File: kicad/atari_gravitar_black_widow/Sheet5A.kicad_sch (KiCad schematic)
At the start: 121 parts, among them Q2 2N6044, Q3 2N6044, Q4 2N6044

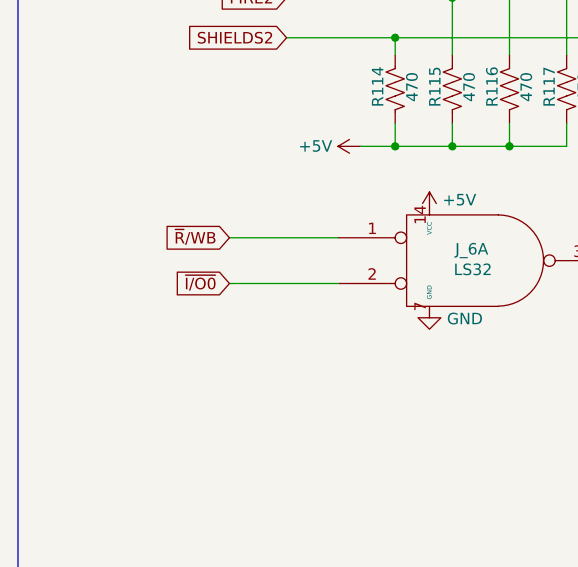
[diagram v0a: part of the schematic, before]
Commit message: Row 3 - 3.5 tracess
Also fixed some schematic errors (IO at J6, power at R4, Z out TP)
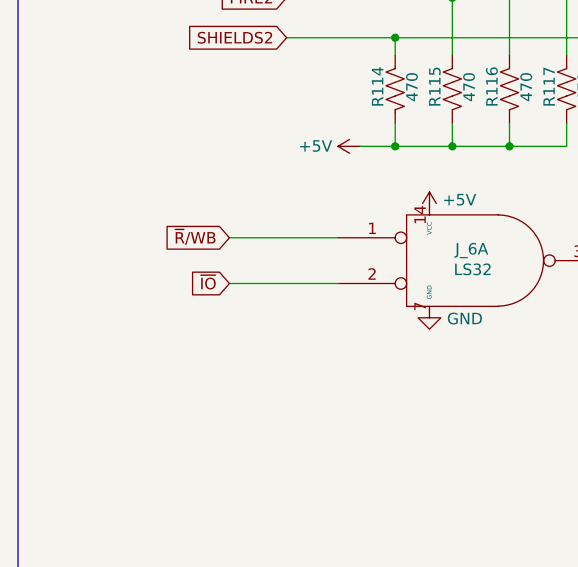
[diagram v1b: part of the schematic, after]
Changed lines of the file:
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@@
     )
   )
-  (global_label "~{I{slash}O0}" (shape input) (at 61.595 146.05 180) (fields_autoplaced)
+  (global_label "~{IO}" (shape input) (at 61.595 146.05 180) (fields_autoplaced)
     (effects (font (size 1.27 1.27)) (justify right))
-    (property "Intersheet References" "${INTERSHEET_REFS}" (id 0) (at 54.7956 145.9706 0)
+    (property "Intersheet References" "${INTERSHEET_REFS}" (id 0) (at 57.3356 145.9706 0)
       (effects (font (size 1.27 1.27)) (justify right) hide)
     )

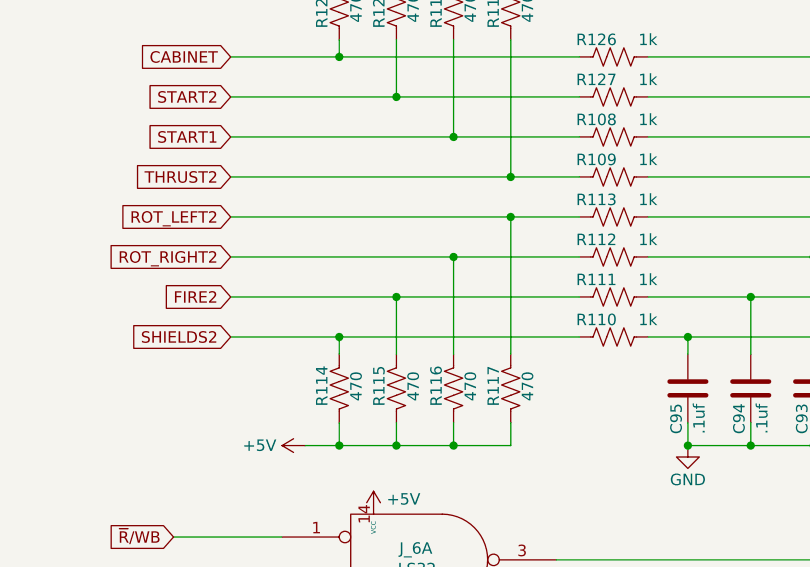
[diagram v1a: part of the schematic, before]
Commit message: fixed coin door schematic issues
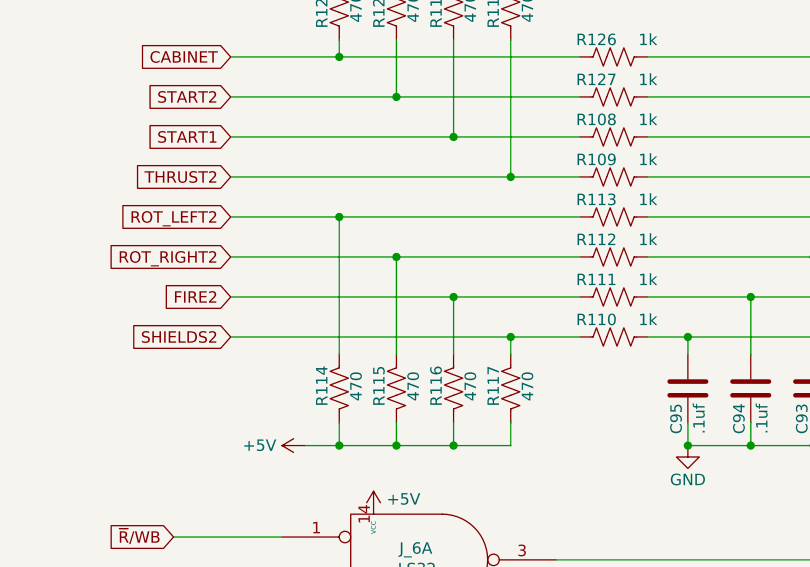
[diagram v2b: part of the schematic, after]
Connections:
- net FIRE2: now also R116.2; no longer R115.2
- net ROT_LEFT2: now also R114.2; no longer R117.2
- net ROT_RIGHT2: now also R115.2; no longer R116.2
- net SHIELDS2: now also R117.2; no longer R114.2
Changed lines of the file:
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@@
   (junction (at 499.745 117.475) (diameter 0) (color 0 0 0 0)
   )
+  (junction (at 92.71 114.3) (diameter 0) (color 0 0 0 0)
+  )
   (junction (at 167.005 87.63) (diameter 0) (color 0 0 0 0)
   )
@@
   (junction (at 327.66 145.415) (diameter 0) (color 0 0 0 0)
   )
+  (junction (at 86.36 109.855) (diameter 0) (color 0 0 0 0)
+  )
   (junction (at 296.545 47.625) (diameter 0) (color 0 0 0 0)
   )
@@
   (junction (at 160.02 92.075) (diameter 0) (color 0 0 0 0)
   )
+  (junction (at 80.01 105.41) (diameter 0) (color 0 0 0 0)
+  )
   (junction (at 118.745 300.355) (diameter 0) (color 0 0 0 0)
   )
@@
   (junction (at 296.545 127.635) (diameter 0) (color 0 0 0 0)
   )
-  (junction (at 80.01 118.745) (diameter 0) (color 0 0 0 0)
-  )
   (junction (at 276.225 67.945) (diameter 0) (color 0 0 0 0)
   )
@@
   (junction (at 153.035 96.52) (diameter 0) (color 0 0 0 0)
   )
-  (junction (at 86.36 114.3) (diameter 0) (color 0 0 0 0)
-  )
   (junction (at 86.36 237.49) (diameter 0) (color 0 0 0 0)
   )
@@
   (junction (at 314.325 75.565) (diameter 0) (color 0 0 0 0)
   )
-  (junction (at 92.71 109.855) (diameter 0) (color 0 0 0 0)
-  )
   (junction (at 377.19 314.325) (diameter 0) (color 0 0 0 0)
   )
@@
   (junction (at 139.7 237.49) (diameter 0) (color 0 0 0 0)
   )
+  (junction (at 99.06 118.745) (diameter 0) (color 0 0 0 0)
+  )
   (junction (at 104.775 300.355) (diameter 0) (color 0 0 0 0)
-  )
-  (junction (at 99.06 105.41) (diameter 0) (color 0 0 0 0)
   )
   (junction (at 314.325 137.795) (diameter 0) (color 0 0 0 0)
@@
     (stroke (width 0) (type default) (color 0 0 0 0))
   )
-  (wire (pts (xy 67.945 109.855) (xy 92.71 109.855))
-    (stroke (width 0) (type default) (color 0 0 0 0))
-  )
   (wire (pts (xy 294.64 70.485) (xy 305.435 70.485))
     (stroke (width 0) (type default) (color 0 0 0 0))
   )
-  (wire (pts (xy 67.945 118.745) (xy 80.01 118.745))
-    (stroke (width 0) (type default) (color 0 0 0 0))
-  )
   (wire (pts (xy 160.02 130.81) (xy 160.02 128.27))
     (stroke (width 0) (type default) (color 0 0 0 0))
@@
     (stroke (width 0) (type default) (color 0 0 0 0))
   )
+  (wire (pts (xy 92.71 114.3) (xy 106.68 114.3))
+    (stroke (width 0) (type default) (color 0 0 0 0))
+  )
   (wire (pts (xy 341.63 127.635) (xy 296.545 127.635))
     (stroke (width 0) (type default) (color 0 0 0 0))
   )
-  (wire (pts (xy 86.36 120.65) (xy 86.36 114.3))
-    (stroke (width 0) (type default) (color 0 0 0 0))
-  )
   (wire (pts (xy 92.71 327.66) (xy 101.6 327.66))
     (stroke (width 0) (type default) (color 0 0 0 0))
   )
-  (wire (pts (xy 67.945 105.41) (xy 99.06 105.41))
-    (stroke (width 0) (type default) (color 0 0 0 0))
-  )
   (wire (pts (xy 76.2 130.81) (xy 80.01 130.81))
     (stroke (width 0) (type default) (color 0 0 0 0))
@@
     (stroke (width 0) (type default) (color 0 0 0 0))
   )
+  (wire (pts (xy 80.01 105.41) (xy 80.01 120.65))
+    (stroke (width 0) (type default) (color 0 0 0 0))
+  )
   (wire (pts (xy 294.64 140.335) (xy 318.77 140.335))
     (stroke (width 0) (type default) (color 0 0 0 0))
@@
     (stroke (width 0) (type default) (color 0 0 0 0))
   )
-  (wire (pts (xy 67.945 114.3) (xy 86.36 114.3))
-    (stroke (width 0) (type default) (color 0 0 0 0))
-  )
   (wire (pts (xy 67.945 314.325) (xy 73.66 314.325))
     (stroke (width 0) (type default) (color 0 0 0 0))
@@
     (stroke (width 0) (type default) (color 0 0 0 0))
   )
-  (wire (pts (xy 99.06 105.41) (xy 99.06 120.65))
-    (stroke (width 0) (type default) (color 0 0 0 0))
-  )
   (wire (pts (xy 139.7 309.88) (xy 139.7 297.18))
     (stroke (width 0) (type default) (color 0 0 0 0))
@@
     (stroke (width 0) (type default) (color 0 0 0 0))
   )
-  (wire (pts (xy 92.71 109.855) (xy 106.68 109.855))
+  (wire (pts (xy 67.945 109.855) (xy 86.36 109.855))
     (stroke (width 0) (type default) (color 0 0 0 0))
   )
@@
     (stroke (width 0) (type default) (color 0 0 0 0))
   )
+  (wire (pts (xy 99.06 118.745) (xy 106.68 118.745))
+    (stroke (width 0) (type default) (color 0 0 0 0))
+  )
   (wire (pts (xy 314.325 75.565) (xy 341.63 75.565))
     (stroke (width 0) (type default) (color 0 0 0 0))
@@
     (stroke (width 0) (type default) (color 0 0 0 0))
   )
+  (wire (pts (xy 86.36 109.855) (xy 86.36 120.65))
+    (stroke (width 0) (type default) (color 0 0 0 0))
+  )
   (wire (pts (xy 471.17 177.165) (xy 473.075 177.165))
     (stroke (width 0) (type default) (color 0 0 0 0))
@@
     (stroke (width 0) (type default) (color 0 0 0 0))
   )
+  (wire (pts (xy 80.01 105.41) (xy 106.68 105.41))
+    (stroke (width 0) (type default) (color 0 0 0 0))
+  )
   (polyline (pts (xy 231.14 38.1) (xy 231.14 370.205))
     (stroke (width 0) (type default) (color 0 0 0 0))
@@
     (stroke (width 0) (type default) (color 0 0 0 0))
   )
-  (wire (pts (xy 99.06 105.41) (xy 106.68 105.41))
+  (wire (pts (xy 67.945 105.41) (xy 80.01 105.41))
     (stroke (width 0) (type default) (color 0 0 0 0))
   )
@@
     (stroke (width 0) (type default) (color 0 0 0 0))
   )
-  (wire (pts (xy 80.01 118.745) (xy 106.68 118.745))
+  (wire (pts (xy 67.945 118.745) (xy 99.06 118.745))
     (stroke (width 0) (type default) (color 0 0 0 0))
   )
@@
     (stroke (width 0) (type default) (color 0 0 0 0))
   )
+  (wire (pts (xy 92.71 114.3) (xy 92.71 120.65))
+    (stroke (width 0) (type default) (color 0 0 0 0))
+  )
   (wire (pts (xy 279.4 75.565) (xy 276.225 75.565))
     (stroke (width 0) (type default) (color 0 0 0 0))
@@
     (stroke (width 0) (type default) (color 0 0 0 0))
   )
-  (wire (pts (xy 80.01 120.65) (xy 80.01 118.745))
-    (stroke (width 0) (type default) (color 0 0 0 0))
-  )
   (wire (pts (xy 469.265 177.165) (xy 471.17 177.165))
     (stroke (width 0) (type default) (color 0 0 0 0))
@@
     (stroke (width 0) (type default) (color 0 0 0 0))
   )
-  (wire (pts (xy 86.36 114.3) (xy 106.68 114.3))
+  (wire (pts (xy 67.945 114.3) (xy 92.71 114.3))
     (stroke (width 0) (type default) (color 0 0 0 0))
   )
@@
     (stroke (width 0) (type default) (color 0 0 0 0))
   )
-  (wire (pts (xy 92.71 109.855) (xy 92.71 120.65))
-    (stroke (width 0) (type default) (color 0 0 0 0))
-  )
   (wire (pts (xy 67.945 220.98) (xy 80.01 220.98))
     (stroke (width 0) (type default) (color 0 0 0 0))
@@
     (stroke (width 0) (type default) (color 0 0 0 0))
   )
+  (wire (pts (xy 86.36 109.855) (xy 106.68 109.855))
+    (stroke (width 0) (type default) (color 0 0 0 0))
+  )
   (wire (pts (xy 377.19 285.75) (xy 359.41 285.75))
     (stroke (width 0) (type default) (color 0 0 0 0))
@@
     (stroke (width 0) (type default) (color 0 0 0 0))
   )
+  (wire (pts (xy 99.06 118.745) (xy 99.06 120.65))
+    (stroke (width 0) (type default) (color 0 0 0 0))
+  )

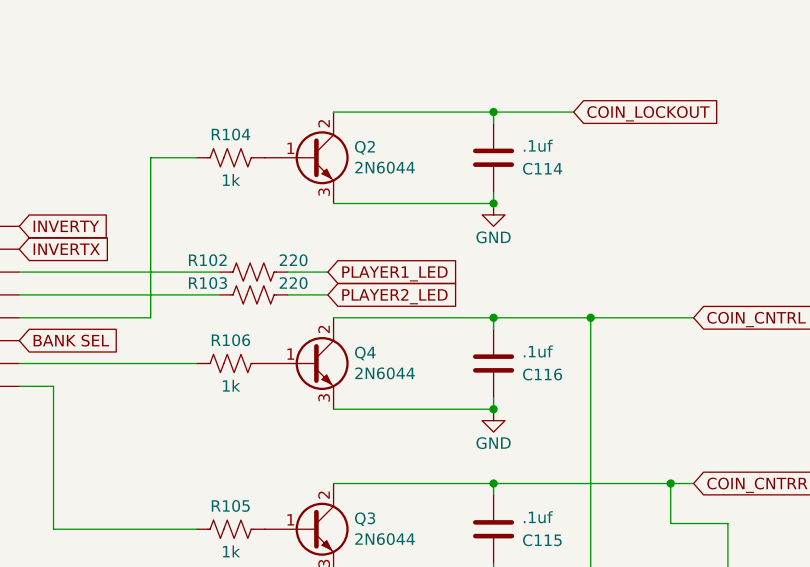
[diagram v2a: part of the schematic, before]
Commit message: player 1 led issue fixed
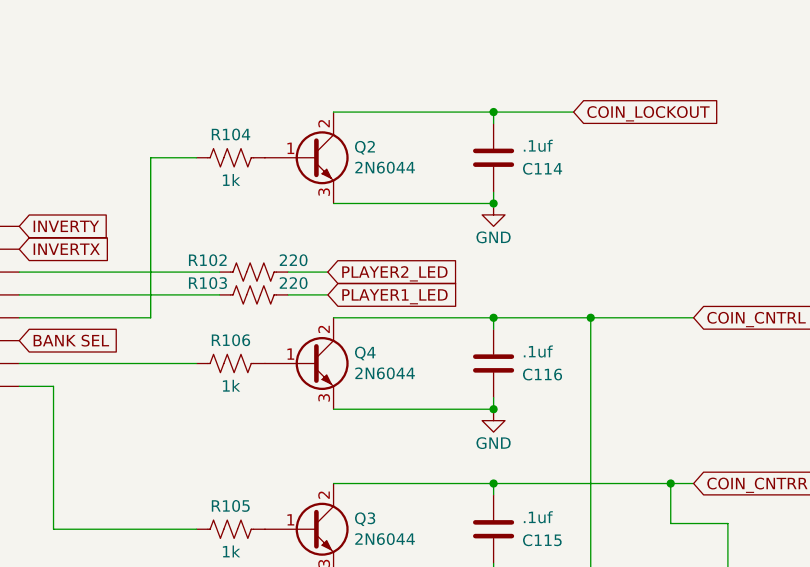
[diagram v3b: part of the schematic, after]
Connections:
- net PLAYER1_LED: no longer R102.1
- net PLAYER2_LED: now also R102.1; no longer R103.1
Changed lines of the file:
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@@
     )
   )
-  (global_label "PLAYER1_LED" (shape input) (at 358.775 280.67 0) (fields_autoplaced)
-    (effects (font (size 1.27 1.27)) (justify left))
-    (property "Intersheet References" "${INTERSHEET_REFS}" (id 0) (at 373.6178 280.5906 0)
+  (global_label "PLAYER1_LED" (shape input) (at 358.78 283.21 0) (fields_autoplaced)
+    (effects (font (size 1.27 1.27)) (justify left))
+    (property "Intersheet References" "${INTERSHEET_REFS}" (id 0) (at 373.6228 283.1306 0)
       (effects (font (size 1.27 1.27)) (justify left) hide)
     )
@@
     )
   )
-  (global_label "PLAYER2_LED" (shape input) (at 358.775 283.21 0) (fields_autoplaced)
-    (effects (font (size 1.27 1.27)) (justify left))
-    (property "Intersheet References" "${INTERSHEET_REFS}" (id 0) (at 373.6178 283.1306 0)
-      (effects (font (size 1.27 1.27)) (justify left) hide)
-    )
+  (global_label "PLAYER2_LED" (shape input) (at 358.77 280.67 0) (fields_autoplaced)
+    (effects (font (size 1.27 1.27)) (justify left))
+    (property "Intersheet References" "${INTERSHEET_REFS}" (id 0) (at 373.6128 280.5906 0)
+      (effects (font (size 1.27 1.27)) (justify left) hide)
+    )

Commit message: push
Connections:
- net PLAYER1_LED: now also R103.1
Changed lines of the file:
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@@
     )
   )
-  (global_label "PLAYER1_LED" (shape input) (at 358.78 283.21 0) (fields_autoplaced)
-    (effects (font (size 1.27 1.27)) (justify left))
-    (property "Intersheet References" "${INTERSHEET_REFS}" (id 0) (at 373.6228 283.1306 0)
+  (global_label "PLAYER1_LED" (shape input) (at 358.775 283.21 0) (fields_autoplaced)
+    (effects (font (size 1.27 1.27)) (justify left))
+    (property "Intersheet References" "${INTERSHEET_REFS}" (id 0) (at 373.6178 283.1306 0)
       (effects (font (size 1.27 1.27)) (justify left) hide)
     )
@@
     )
   )
-  (global_label "PLAYER2_LED" (shape input) (at 358.77 280.67 0) (fields_autoplaced)
-    (effects (font (size 1.27 1.27)) (justify left))
-    (property "Intersheet References" "${INTERSHEET_REFS}" (id 0) (at 373.6128 280.5906 0)
-      (effects (font (size 1.27 1.27)) (justify left) hide)
-    )
+  (global_label "PLAYER2_LED" (shape input) (at 358.775 280.67 0) (fields_autoplaced)
+    (effects (font (size 1.27 1.27)) (justify left))
+    (property "Intersheet References" "${INTERSHEET_REFS}" (id 0) (at 373.6178 280.5906 0)
+      (effects (font (size 1.27 1.27)) (justify left) hide)
+    )

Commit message: lots o' traces
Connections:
- net AUD2: now also B_5.2 (-); no longer B_5.3 (+)
- net at B_5.8, R52.1, R53.2: now also B_5.3 (+); no longer B_5.2 (-)
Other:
- note added: "- -"
- note added: "- - - as drawn (erroneously) in Atari SP-206."
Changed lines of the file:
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@@
-    (stroke (width 0) (type default) (color 0 0 0 0))
-  )
-  (wire (pts (xy 497.84 177.8) (xy 506.73 177.8))
     (stroke (width 0) (type default) (color 0 0 0 0))
   )
@@
     (stroke (width 0) (type default) (color 0 0 0 0))
   )
+  (wire (pts (xy 506.73 177.8) (xy 501.65 182.88))
+    (stroke (width 0) (type default) (color 0 0 0 0))
+  )
   (wire (pts (xy 279.4 83.185) (xy 276.225 83.185))
     (stroke (width 0) (type default) (color 0 0 0 0))
@@
     (stroke (width 0) (type default) (color 0 0 0 0))
   )
+  (wire (pts (xy 497.84 177.8) (xy 501.4885 177.8024))
+    (stroke (width 0) (type default) (color 0 0 0 0))
+  )
   (wire (pts (xy 358.775 283.21) (xy 354.33 283.21))
     (stroke (width 0) (type default) (color 0 0 0 0))
@@
     (stroke (width 0) (type default) (color 0 0 0 0))
   )
+  (wire (pts (xy 501.4885 177.8024) (xy 506.73 182.88))
+    (stroke (width 0) (type default) (color 0 0 0 0))
+  )
   (wire (pts (xy 80.01 75.565) (xy 86.36 75.565))
     (stroke (width 0) (type default) (color 0 0 0 0))
@@
   )
   (wire (pts (xy 387.985 285.75) (xy 377.19 285.75))
-    (stroke (width 0) (type default) (color 0 0 0 0))
-  )
-  (wire (pts (xy 501.65 182.88) (xy 506.73 182.88))
     (stroke (width 0) (type default) (color 0 0 0 0))
   )
@@
     (effects (font (size 5.08 5.08) (thickness 1.016) bold) (justify left bottom))
   )
+  (text "- - -  as drawn\n(erroneously) in\nAtari SP-206." (at 493.7567 176.3833 0)
+    (effects (font (size 0.8 0.8)) (justify left bottom))
+  )
   (text "Coin Door and Control Panel Output" (at 270.51 248.92 0)
     (effects (font (size 5.08 5.08) (thickness 0.508) bold) (justify left bottom))
   )
+  (text "- -" (at 502.0415 183.6876 0)
+    (effects (font (size 1.27 1.27)) (justify left bottom))
+  )
+  (text "- -" (at 502.0617 178.5962 0)
+    (effects (font (size 1.27 1.27)) (justify left bottom))
+  )
   (global_label "DB1" (shape input) (at 212.725 114.3 0) (fields_autoplaced)

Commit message: All digital done!
Need ground flood and analog section.
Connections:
- net -15V: now also C29.1, D_5.11 (V-)
- net GND: no longer C29.1, D_5.11 (V-)
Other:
- note added: "Atari SP-206 erroneously shows D5p11 to GND."
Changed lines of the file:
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@@
   (junction (at 511.81 187.96) (diameter 0) (color 0 0 0 0)
   )
+  (junction (at 416.56 120.015) (diameter 0) (color 0 0 0 0)
+  )
   (junction (at 153.035 96.52) (diameter 0) (color 0 0 0 0)
   )
@@
   (junction (at 377.19 273.05) (diameter 0) (color 0 0 0 0)
   )
-  (junction (at 416.56 120.015) (diameter 0) (color 0 0 0 0)
-  )
   (junction (at 189.23 250.19) (diameter 0) (color 0 0 0 0)
   )
@@
     (stroke (width 0) (type default) (color 0 0 0 0))
   )
-  (wire (pts (xy 429.26 120.015) (xy 416.56 120.015))
+  (wire (pts (xy 416.56 120.015) (xy 429.26 120.015))
     (stroke (width 0) (type default) (color 0 0 0 0))
   )
@@
     (effects (font (size 1.27 1.27)) (justify left bottom))
   )
+  (text "Atari SP-206 \nerroneously shows\nD5p11 to GND." (at 423.4227 127.7828 0)
+    (effects (font (size 0.8 0.8)) (justify left bottom))
+  )
   (text "- -" (at 502.0617 178.5962 0)
     (effects (font (size 1.27 1.27)) (justify left bottom))
@@
     (pin "2")
   )
-  (symbol (lib_id "power:GND") (at 416.56 120.015 0) (unit 1)
-    (in_bom yes) (on_board yes)
-    (property "Reference" "#PWR0511" (id 0) (at 416.56 126.365 0)
-      (effects (font (size 1.27 1.27)) hide)
-    )
-    (property "Value" "GND" (id 1) (at 416.56 123.825 0))
-    (property "Footprint" "" (id 2) (at 416.56 120.015 0)
-      (effects (font (size 1.27 1.27)) hide)
-    )
-    (property "Datasheet" "" (id 3) (at 416.56 120.015 0)
-      (effects (font (size 1.27 1.27)) hide)
-    )
-    (pin "1")
-  )
   (symbol (lib_id "power:GND") (at 139.7 237.49 0) (unit 1)
     (in_bom yes) (on_board yes)
@@
       (effects (font (size 1.27 1.27)) hide)
     )
+    (pin "1")
+  )
+  (symbol (lib_id "atari_gravitar_black_widow-cache:power_-15V") (at 416.56 120.015 180) (unit 1)
+    (in_bom yes) (on_board yes) (fields_autoplaced)
+    (property "Reference" "#PWR0511" (id 0) (at 416.56 122.555 0)
+      (effects (font (size 1.27 1.27)) hide)
+    )
+    (property "Value" "power_-15V" (id 1) (at 416.56 124.5775 0))
+    (property "Footprint" "" (id 2) (at 416.56 120.015 0)
+      (effects (font (size 1.27 1.27)) hide)
+    )
+    (property "Datasheet" "" (id 3) (at 416.56 120.015 0)
+      (effects (font (size 1.27 1.27)) hide)
+    )
